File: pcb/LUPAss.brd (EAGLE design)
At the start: 41.6 x 78.7 mm, 22 parts, among them CON1 1, CON2 2

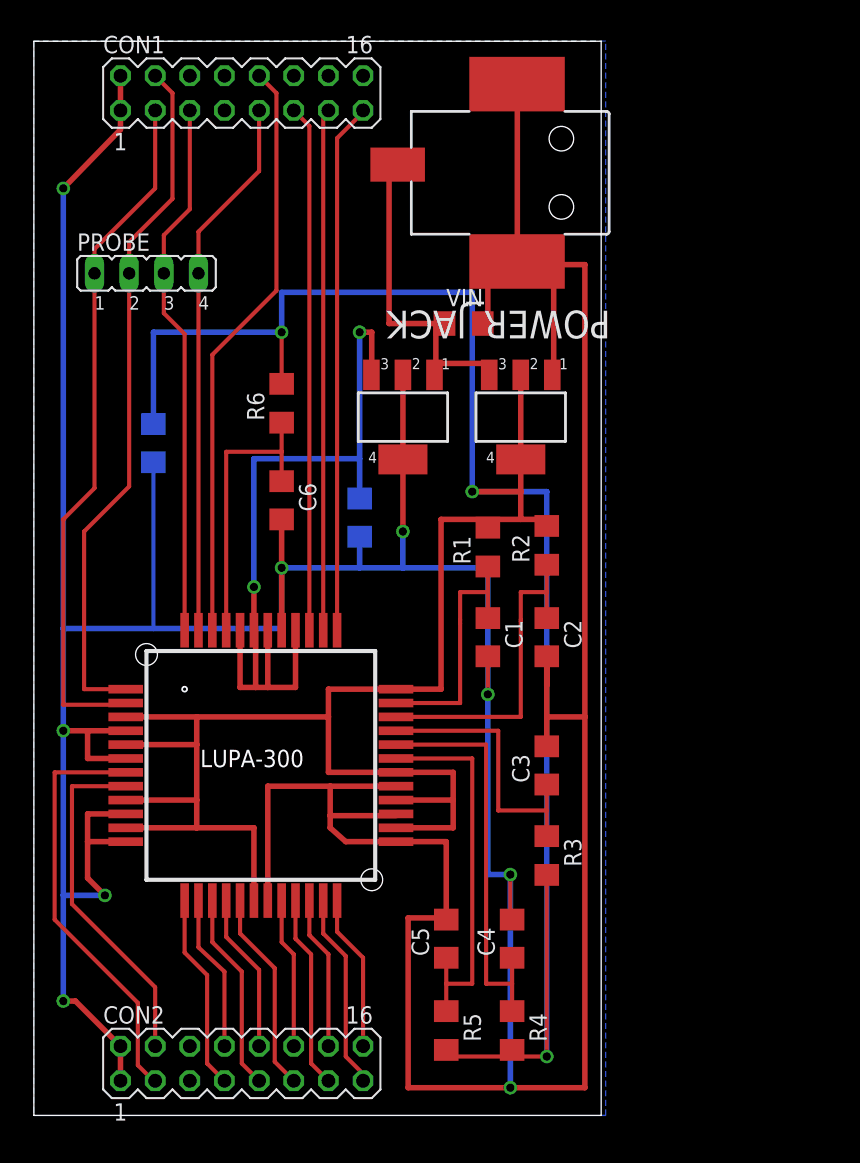
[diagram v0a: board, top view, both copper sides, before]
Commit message: added newer soft start board for pin reference, removed old dual header design
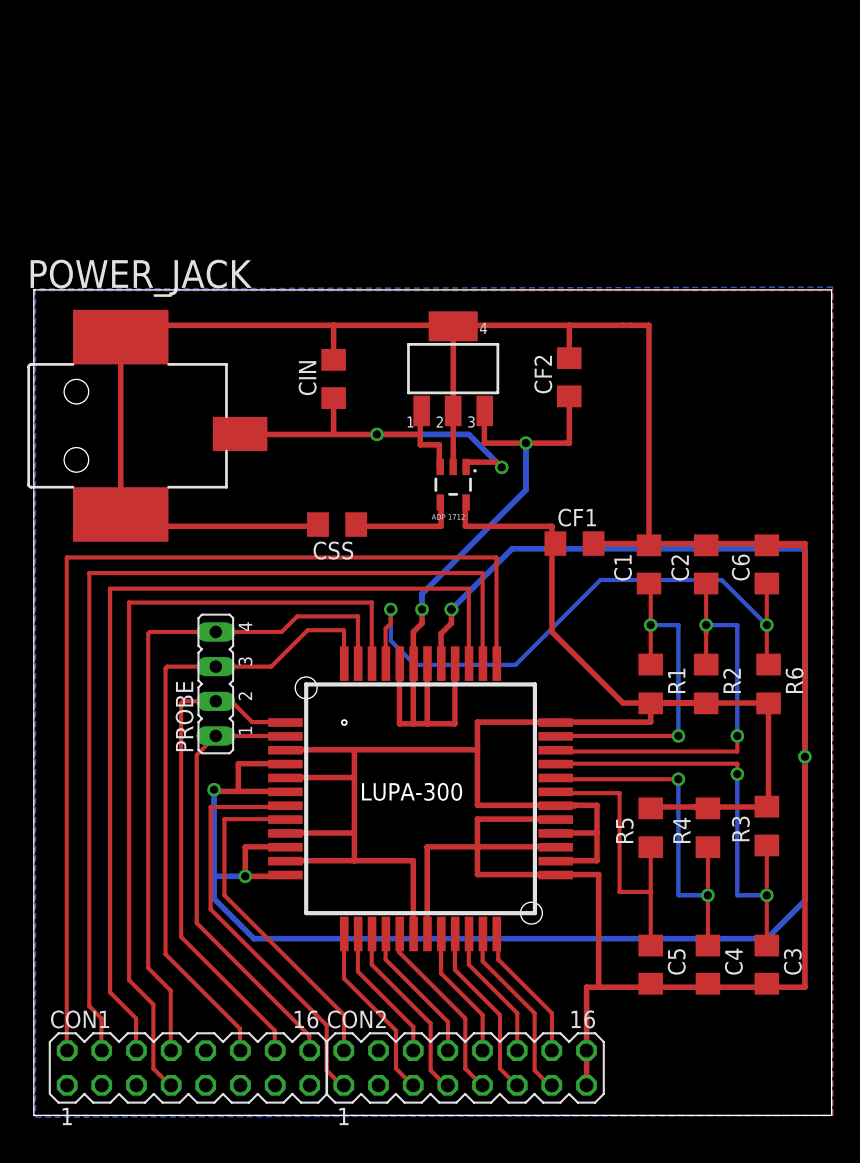
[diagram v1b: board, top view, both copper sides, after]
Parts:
- removed VIN: 100nF, resistor:C3216
- added CIN: 2.2uF, resistor:C3216
- added CSS: 2pF, resistor:C3216
- CF1: value 10uF -> 2.2uF
- U$1: device lupa300:LUPA300 -> LUPA300:LUPA300
- U$2: value LD1117S25 -> ADP1712; device LD1117S25:SOT223 -> ADP1712:SOT23-5
- moved CON1 71.6 mm to (11.3, 3.48)
- moved POWER_JACK 46.4 mm to (-0.38, 50.5), turned to 0 degrees
- moved R6 41.2 mm to (53.8, 31.6), turned to 270 degrees
- moved C6 35.9 mm to (53.7, 40.4), turned to 90 degrees
- moved CF1 31.7 mm to (39.6, 41.9), flipped to the top, turned to 0 degrees
- moved PROBE 30.5 mm to (13.3, 31.6), turned to 90 degrees
- moved C3 21.8 mm to (53.7, 11.0), turned to 270 degrees
- moved R5 21.1 mm to (45.2, 21.1), turned to 90 degrees
- moved R4 20.7 mm to (49.4, 21.1), turned to 90 degrees
- moved CF2 18.5 mm to (39.2, 54.1), flipped to the top, turned to 90 degrees
- moved CON2 16.4 mm to (31.6, 3.48)
- moved R3 16.3 mm to (53.7, 21.2), turned to 90 degrees
- moved R1 15.6 mm to (45.2, 31.6), turned to 270 degrees
- moved R2 15.5 mm to (49.3, 31.6), turned to 270 degrees
- moved C5 15.1 mm to (45.2, 11.0), turned to 270 degrees
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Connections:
- removed net N$11: POWER_JACK.1, U$2.3, U$3.1, VIN.1
- new net IN: CIN.1, POWER_JACK.1, U$2.1, U$2.3, U$3.1
- new net SS: CSS.1, U$2.4
- net 2.5V: now also U$2.5; no longer U$2.2, U$2.4
- net CLK: now also CON2.2; no longer CON2.4
- net D0: now also CON2.5; no longer CON2.7
- net D1: now also CON2.6; no longer CON2.8
- net D2: now also CON2.7; no longer CON2.9
- net D3: now also CON2.8; no longer CON2.10
- net D4: now also CON2.9; no longer CON2.11
- net D5: now also CON2.10; no longer CON2.12
- net D6: now also CON2.11; no longer CON2.13
- net D7: now also CON2.12; no longer CON2.14
- net D8: now also CON2.13; no longer CON2.15
- net D9: now also CON2.14; no longer CON2.16
- net FRAME_VALID: now also CON1.8; no longer CON1.9
- net GND: now also CIN.2, CON2.15, CON2.16, CSS.2, U$2.2; no longer CON1.1, CON1.2, CON2.1, CON2.2, U$2.1, VIN.2
- net INT_TIME1: now also CON1.16; no longer CON1.3
- net INT_TIME2: now also CON1.14; no longer CON1.4
- net INT_TIME3: now also CON1.12; no longer CON1.5
- net LINE_VALID: now also CON1.7; no longer CON1.10
- net RESET_N: now also CON2.1; no longer CON2.3
- net SPI_CLK: now also CON1.4; no longer CON1.13
- net SPI_DATA: now also CON1.6; no longer CON1.11
- net SPI_EN: now also CON1.2; no longer CON1.15
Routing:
- net 2.5V: track 238.4 -> 144.1 mm, vias 3 -> 0
- net GND: track 390.3 -> 347.7 mm, vias 9 -> 5
- net SPI_EN: track 38.7 -> 75.4 mm
- net IN: track 0.00 -> 34.0 mm, vias 0 -> 2
- net SPI_CLK: track 38.3 -> 71.0 mm
- net SPI_DATA: track 38.4 -> 66.4 mm
- net N$11: track 23.4 -> 0.00 mm
- net N$10: track 21.7 -> 44.6 mm, vias 0 -> 2
- net INT_TIME1: track 50.9 -> 32.2 mm
- net LINE_VALID: track 43.1 -> 59.0 mm
- net INT_TIME2: track 51.2 -> 36.8 mm
- net N$7: track 21.1 -> 32.4 mm, vias 0 -> 2
- net FRAME_VALID: track 39.6 -> 50.7 mm
- net SS: track 0.00 -> 7.62 mm
- net INT_TIME3: track 39.5 -> 46.9 mm
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- added copper zone on layer 1, net GND
- added copper zone on layer 16, net GND
- removed copper zone on layer 16, net N$1
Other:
- board size 41.6 x 78.7 mm -> 58.5 x 60.5 mm
